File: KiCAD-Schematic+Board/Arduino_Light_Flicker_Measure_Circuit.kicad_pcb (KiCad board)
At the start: 2 copper layers, 35.6 x 113 mm, 35 parts, among them J1 Ds, J3 FTDI, J5 PWR(5V), Q1 BC547, Q2 BC547, U1 ATmega328P-PU, U2 AD5242, U3 AD823A, U4 Display

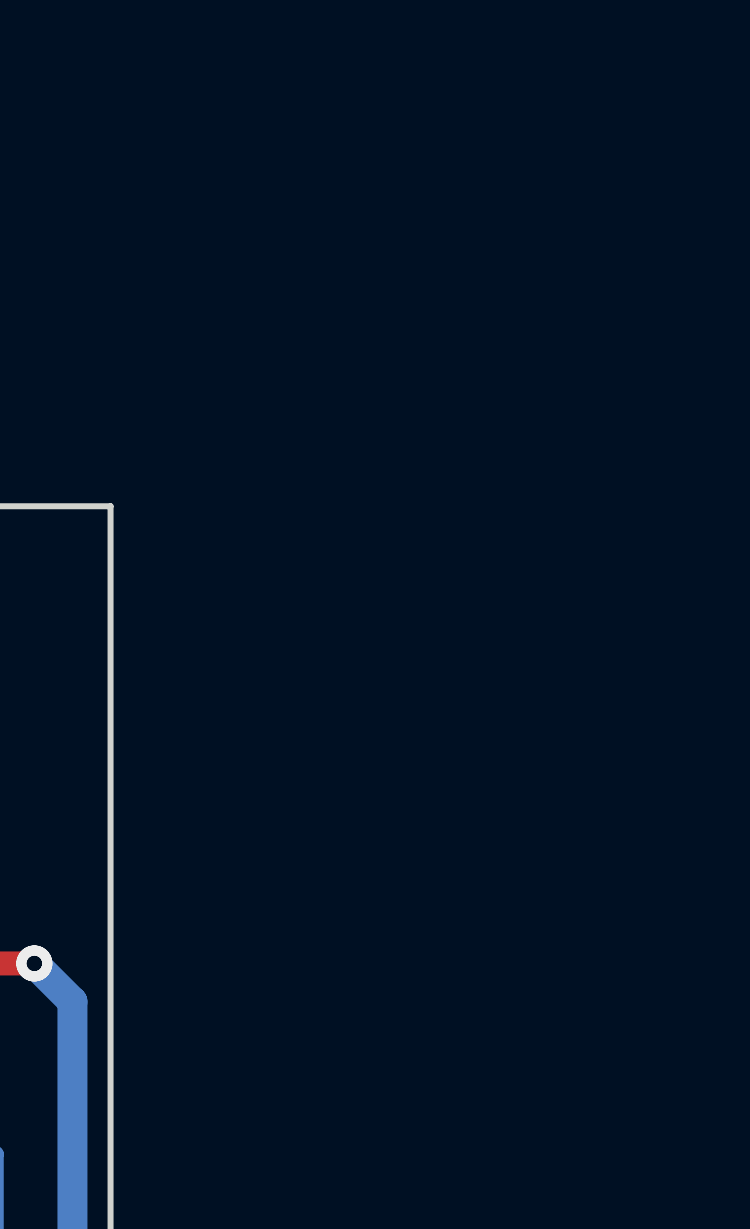
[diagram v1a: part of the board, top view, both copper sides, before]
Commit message: Add SSD1306 file, minor updates, also swapped two pins.  Slowly iterating.
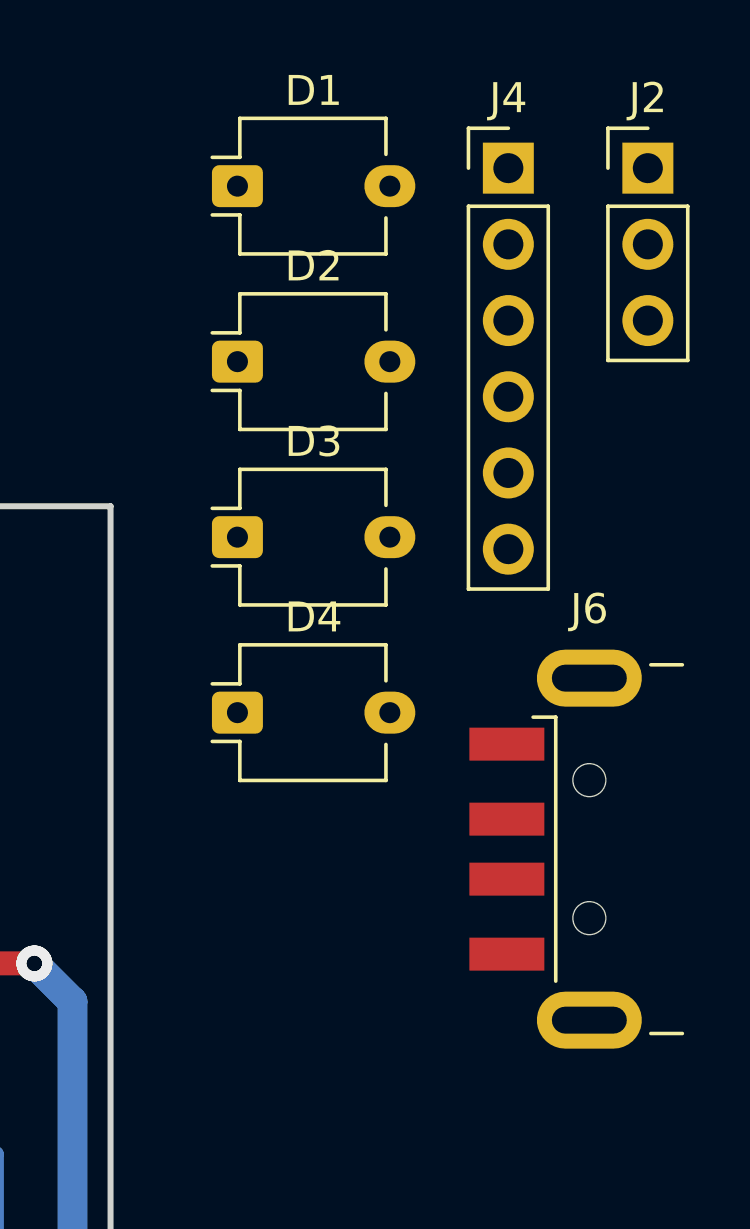
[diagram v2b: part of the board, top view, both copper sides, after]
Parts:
- added D1: BPW34, OptoDevice:Osram_DIL2_4.3x4.65mm_P5.08mm, F.Cu at (88.0, 55.4)
- added D2: BPW34, OptoDevice:Osram_DIL2_4.3x4.65mm_P5.08mm, F.Cu at (88.0, 61.2)
- added D3: BPW34, OptoDevice:Osram_DIL2_4.3x4.65mm_P5.08mm, F.Cu at (88.0, 67.1)
- added D4: BPW34, OptoDevice:Osram_DIL2_4.3x4.65mm_P5.08mm, F.Cu at (88.0, 72.9)
- added J2: Ds, Connector_PinHeader_2.54mm:PinHeader_1x03_P2.54mm_Vertical, F.Cu at (101.7, 54.8)
- added J4: FTDI-Conn, Connector_PinHeader_2.54mm:PinHeader_1x06_P2.54mm_Vertical, F.Cu at (97.1, 54.8)
- added J6: USB Power (5V), Connector_USB:USB_A_CNCTech_1001-011-01101_Horizontal, F.Cu at (106.7, 77.5)
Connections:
- net /TMR1-T1Clock renamed /T1
- J3 pad 4: Net-(J3-Pad4) -> unconnected-(J3-Pin_4-Pad4)
- U1 pad 12: Net-(U1-Pad12) -> unconnected-(U1-PD6-Pad12)
- U1 pad 13: Net-(U1-Pad13) -> unconnected-(U1-PD7-Pad13)
- U1 pad 14: Net-(U1-Pad14) -> unconnected-(U1-PB0-Pad14)
- U1 pad 15: Net-(U1-Pad15) -> unconnected-(U1-PB1-Pad15)
- U1 pad 16: Net-(U1-Pad16) -> unconnected-(U1-PB2-Pad16)
- U1 pad 17: Net-(U1-Pad17) -> unconnected-(U1-PB3-Pad17)
- U1 pad 18: Net-(U1-Pad18) -> unconnected-(U1-PB4-Pad18)
- U1 pad 19: Net-(U1-Pad19) -> unconnected-(U1-PB5-Pad19)
- U1 pad 24: Net-(U1-Pad24) -> unconnected-(U1-PC1-Pad24)
- U1 pad 25: Net-(U1-Pad25) -> unconnected-(U1-PC2-Pad25)
- U1 pad 26: Net-(U1-Pad26) -> unconnected-(U1-PC3-Pad26)
- U1 pad 4: Net-(U1-Pad4) -> unconnected-(U1-PD2-Pad4)
- U1 pad 5: Net-(U1-Pad5) -> unconnected-(U1-PD3-Pad5)
- U1 pad 6: Net-(U1-Pad6) -> unconnected-(U1-PD4-Pad6)
- U2 pad 1: Net-(U2-Pad1) -> unconnected-(U2-O1-Pad1)
- U2 pad 13: Net-(U2-Pad13) -> unconnected-(U2-O2-Pad13)
- U2 pad 16: Net-(U2-Pad16) -> unconnected-(U2-A2-Pad16)
- U2 pad 2: Net-(U2-Pad2) -> unconnected-(U2-A1-Pad2)
- U4 pad 2: GNDD -> +5V

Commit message: Update board setup to be mostly complete.  Still need to shrink and reorganize a bit.
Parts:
- removed J4: FTDI-Conn, Connector_PinHeader_2.54mm:PinHeader_1x06_P2.54mm_Vertical
- C1, C2: moved to B.Cu
- C100: renamed from 16MHz1; value Q -> 16MHz
- R1, R2: value 10k -> 10kΩ
- R11, R7, R9: value 1,5k -> 1.5kΩ
- R4: value 10k -> 10kΩ
- R5: value 1M -> 1MΩ
- R6: value 120k -> 120kΩ
- R8: value 1k -> 1kΩ
- moved J6 95.2 mm to (88.2, 170.8)
- moved J2 39.8 mm to (66.0, 72.4), turned to 90 degrees
- moved C9 5.46 mm to (59.1, 78.1), turned to 90 degrees
- moved C2 4.05 mm to (64.8, 156.2)
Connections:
- net /SCL renamed SCL
- net /SDA renamed SDA
- net /T1 renamed TMR1-T1Clock
- net GNDD renamed GND
- C9 pad 1: +5V -> Net-(U4-GND)
- U4 pad 1: +5V -> Net-(U4-GND)
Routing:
- net GND: track 298.4 -> 37.1 mm, vias 1 -> 0
- net +5V: track 222.1 -> 210.4 mm, vias 9 -> 2
- net SDA: track 107.2 -> 102.3 mm, vias 8 -> 3
- net Net-(U4-GND): track 0.00 -> 4.71 mm
- net Net-(U1-AREF): track 5.61 -> 9.98 mm
- net SCL: track 86.7 -> 84.1 mm, vias 8 -> 3
- net TMR1-T1Clock: track 136.9 -> 134.4 mm, vias 4 -> 2
- net Net-(J1-Pin_3): track 88.6 -> 87.5 mm, vias 7 -> 3
- net /ADC0: vias 4 -> 2

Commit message: Fix broken gitignore due to typo... Ouch.  Also clean up schematic even more, still need to do proper layout and BOM sourcing stuff.  Plus figure out the actual parts for the photodiodes still.
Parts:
- C1, C2, C3: value 100n -> 100nF
- R10: value 100k -> 100kΩ
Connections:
- net /ADC0 renamed ADC0
- C100 pad 1: Net-(U1-XTAL1/PB6) -> GND
- C4 pad 1: Net-(U1-XTAL1/PB6) -> GND
- U1 pad 9: Net-(U1-XTAL1/PB6) -> GND
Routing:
- net Net-(U1-XTAL1/PB6): track 12.3 -> 0.00 mm
- net GND: track 37.1 -> 49.4 mm

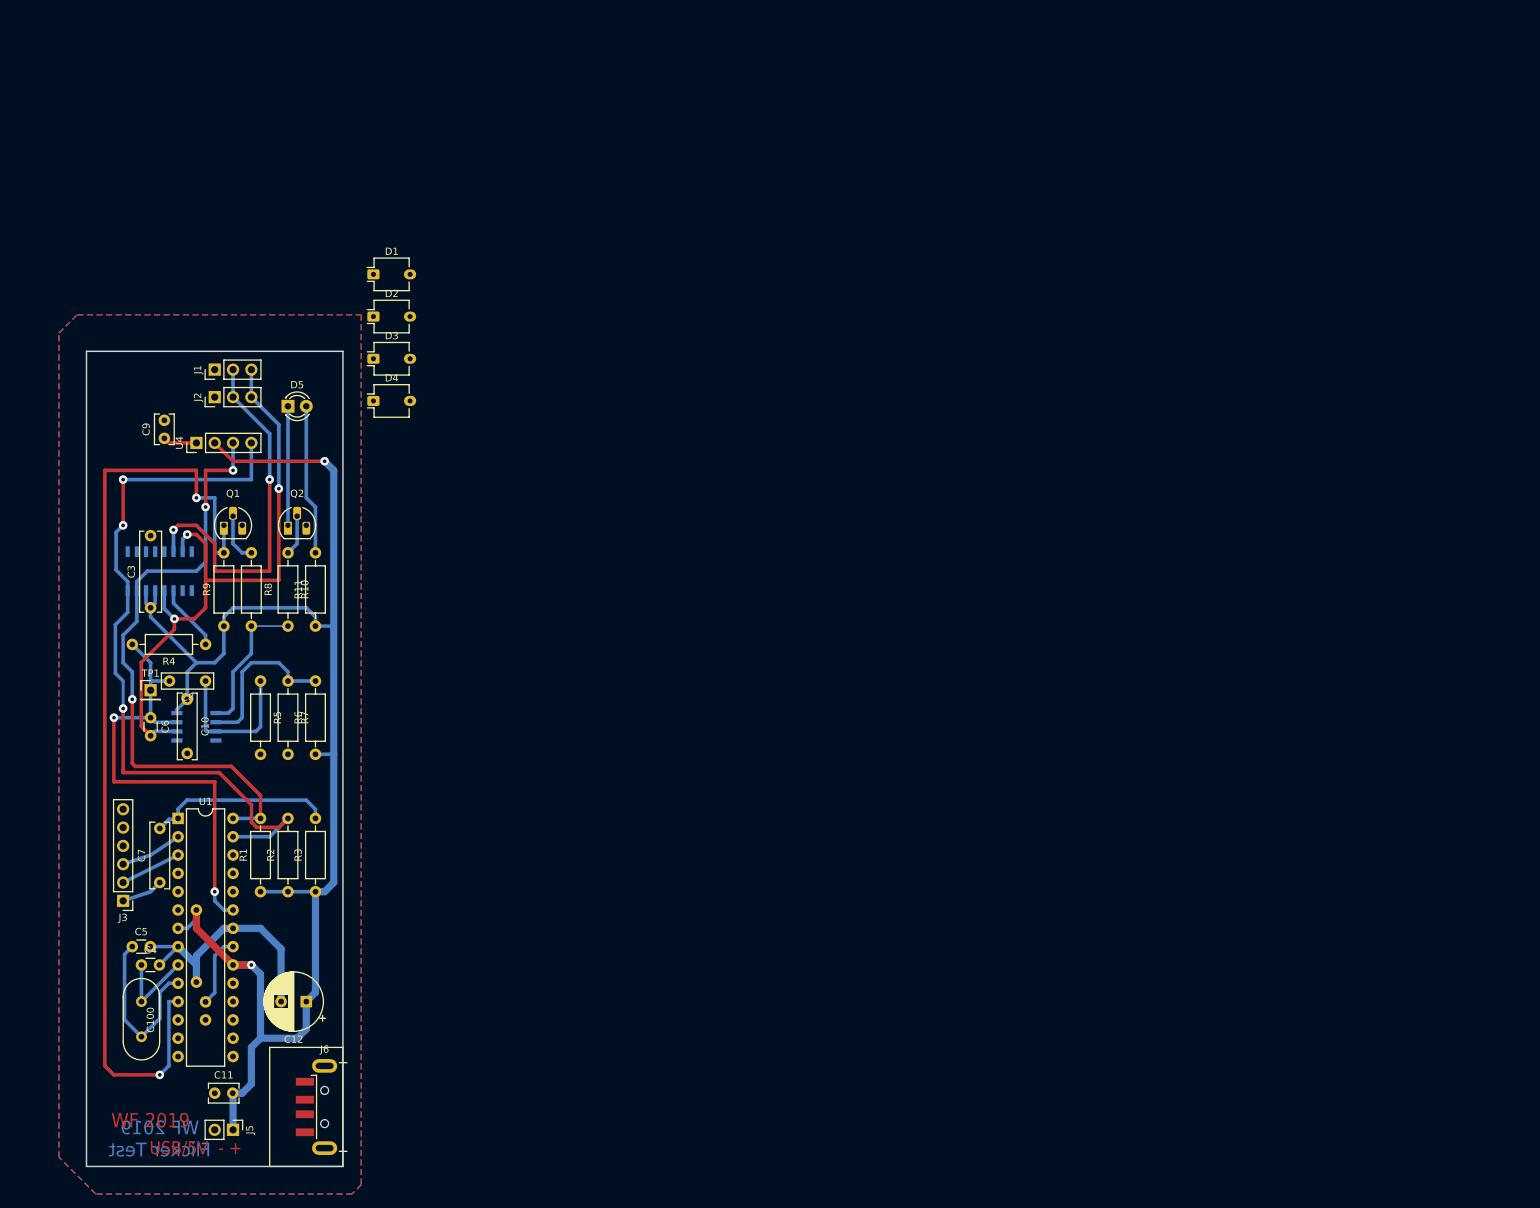
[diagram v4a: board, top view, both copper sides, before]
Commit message: Small update to add Pro Mini footprint to get rid of original footprint stuff hopefully.
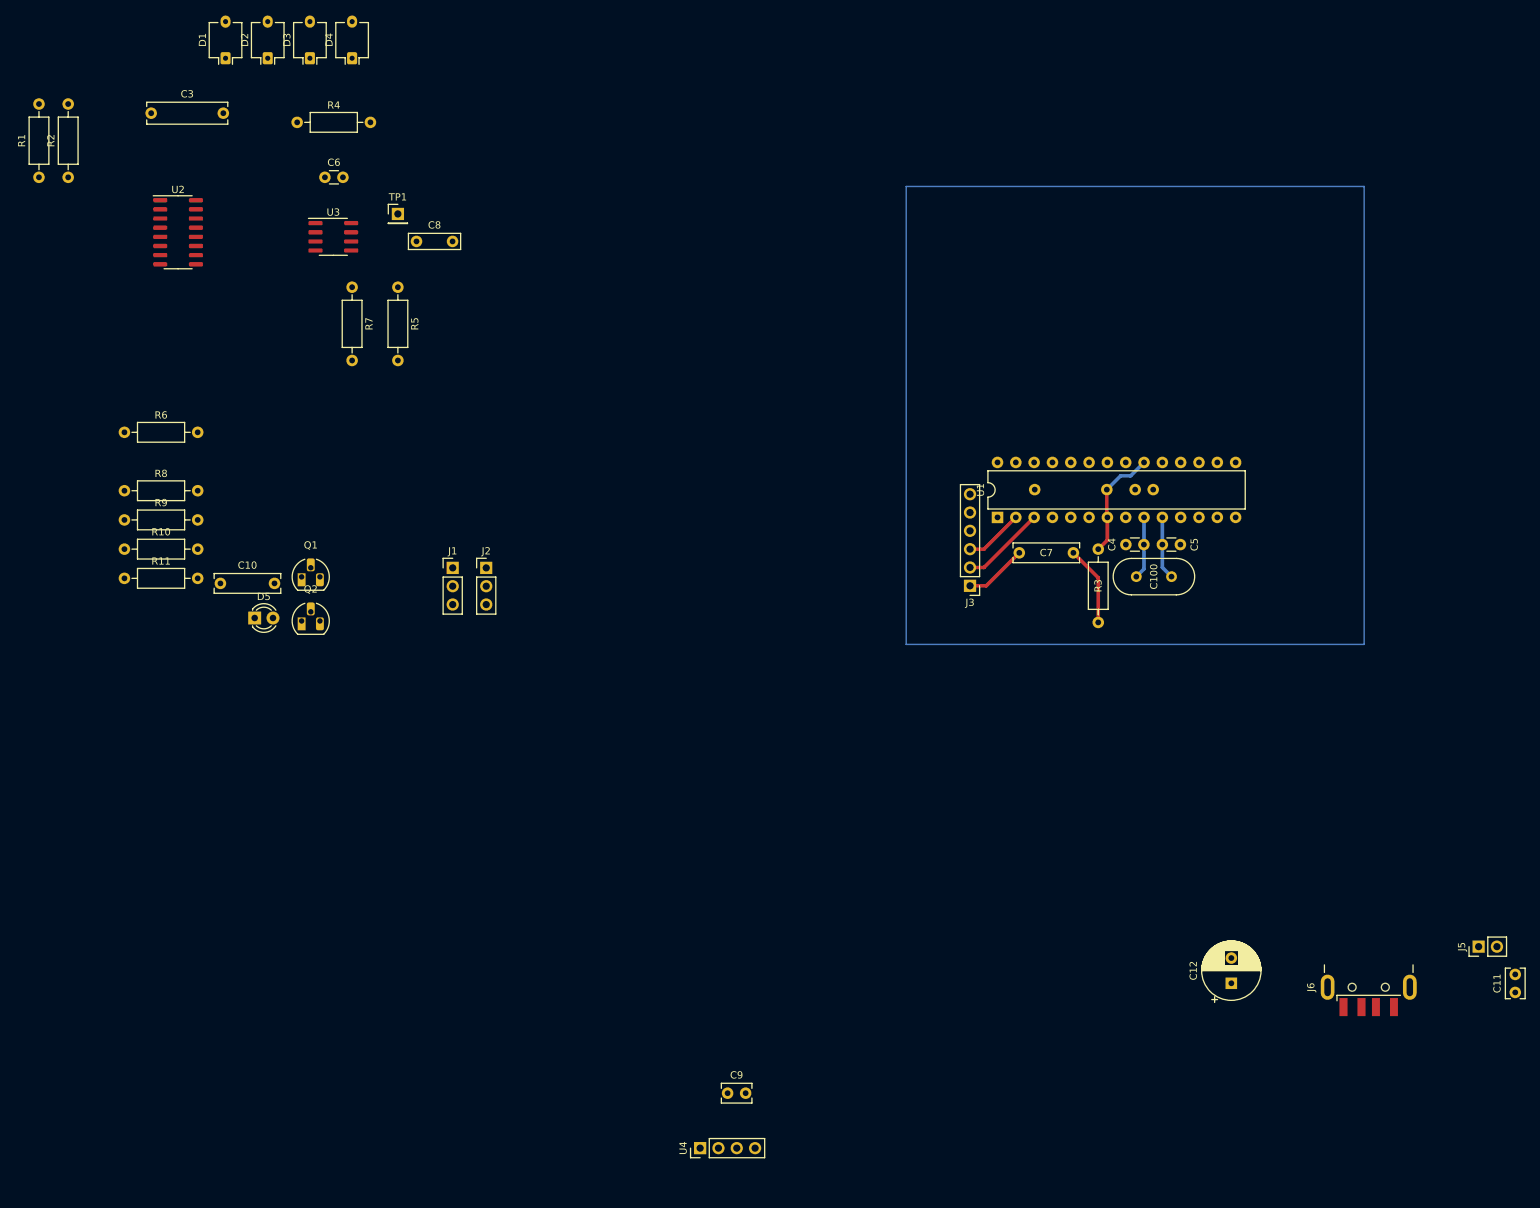
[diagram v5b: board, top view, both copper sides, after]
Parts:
- U2, U3: moved to F.Cu
- moved C11 180.9 mm to (246.4, 154.9), turned to 90 degrees
- moved J5 174.6 mm to (241.3, 148.6), turned to 90 degrees
- moved C5 153.3 mm to (197.4, 92.8)
- moved C4 150.7 mm to (194.9, 92.8), turned to 180 degrees
- moved C100 150.0 mm to (193.8, 97.3), turned to 0 degrees
- moved C2 147.2 mm to (193.7, 85.2), turned to 0 degrees
- moved J6 139.9 mm to (226.1, 147.3), turned to 90 degrees
- moved C1 139.1 mm to (189.7, 85.2), turned to 180 degrees
- moved C12 128.3 mm to (207.0, 153.7), turned to 90 degrees
- moved C7 127.7 mm to (177.6, 94.0), turned to 0 degrees
- moved J3 125.3 mm to (170.8, 98.6)
- moved U1 121.1 mm to (174.6, 89.1), turned to 90 degrees
- moved U4 120.2 mm to (133.3, 176.5)
- moved C9 119.8 mm to (137.2, 168.9), turned to 0 degrees
- moved R3 118.5 mm to (188.6, 93.5), turned to -90 degrees
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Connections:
- C100 pad 1: GND -> Net-(U1-XTAL1/PB6)
- C4 pad 1: GND -> Net-(U1-XTAL1/PB6)
- U1 pad 9: GND -> Net-(U1-XTAL1/PB6)
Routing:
- net +5V: track 210.4 -> 15.5 mm, vias 2 -> 0
- net TMR1-T1Clock: track 134.4 -> 0.00 mm, vias 2 -> 0
- net SDA: track 102.3 -> 0.00 mm, vias 3 -> 0
- net Net-(J1-Pin_3): track 87.5 -> 0.00 mm, vias 3 -> 0
- net SCL: track 84.1 -> 0.00 mm, vias 3 -> 0
- net ADC0: track 65.3 -> 0.00 mm, vias 2 -> 0
- net Net-(J1-Pin_2): track 51.5 -> 0.00 mm, vias 2 -> 0
- net GND: track 49.4 -> 0.00 mm
- net Net-(U3A--): track 22.7 -> 0.00 mm
- net Net-(U3A-+): track 21.1 -> 0.00 mm
- net Net-(D5-A): track 20.8 -> 0.00 mm
- net Net-(R10-Pad2): track 20.2 -> 0.00 mm
- net Net-(D5-K): track 16.5 -> 0.00 mm
- net Net-(U1-XTAL2/PB7): track 24.2 -> 8.74 mm
- net Net-(U1-~{RESET}/PC6): track 25.8 -> 11.1 mm
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- removed copper zone on B.Cu, net GND
- removed copper zone on F.Cu, net GND
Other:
- board outline removed
- board text removed: "USB/5V - +"
- board text removed: "WF 2019"
- board text removed: "WF 2019 Flicker Test"

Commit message: Update to do basic messed-up layout.  Imperfect but hopefully functional.
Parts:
- C10: moved to B.Cu
- moved C11 154.8 mm to (122.4, 62.2), turned to 0 degrees
- moved J5 142.2 mm to (125.7, 65.8), turned to -90 degrees
- moved U4 133.7 mm to (74.2, 56.6), turned to 0 degrees
- moved C9 124.7 mm to (77.6, 59.4), turned to -90 degrees
- moved J6 120.7 mm to (139.3, 63.3), turned to 0 degrees
- moved C12 117.1 mm to (123.0, 72.0), turned to 0 degrees
- moved C100 93.8 mm to (102.3, 76.9)
- moved C2 93.8 mm to (102.1, 64.8)
- moved J3 93.8 mm to (79.2, 78.2)
- moved U1 93.8 mm to (83.0, 68.7)
- moved C1 93.8 mm to (98.2, 64.8)
- moved C4 93.8 mm to (103.3, 72.5)
- moved C5 93.8 mm to (105.9, 72.5)
- moved C7 93.8 mm to (86.0, 73.6)
- moved R3 92.7 mm to (97.3, 77.2), turned to 180 degrees
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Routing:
- net +5V: track 15.5 -> 153.3 mm, vias 0 -> 1
- net ADC0: track 0.00 -> 47.0 mm, vias 0 -> 1
- net Net-(D1-A): track 0.00 -> 45.1 mm
- net Net-(J1-Pin_3): track 0.00 -> 41.2 mm, vias 0 -> 2
- net Net-(R10-Pad2): track 0.00 -> 37.2 mm, vias 0 -> 1
- net SCL: track 0.00 -> 30.3 mm
- net SDA: track 0.00 -> 27.1 mm
- net TMR1-T1Clock: track 0.00 -> 26.5 mm
- net Net-(U3A-+): track 0.00 -> 22.9 mm, vias 0 -> 1
- net Net-(U3A--): track 0.00 -> 21.3 mm
- net Net-(J1-Pin_2): track 0.00 -> 17.0 mm, vias 0 -> 1
- net Net-(U2-W1): track 0.00 -> 16.9 mm, vias 0 -> 1
- net Net-(Q2-B): track 0.00 -> 14.3 mm
- net Net-(D1-K): track 0.00 -> 13.5 mm
- net Net-(U1-~{RESET}/PC6): track 11.1 -> 21.2 mm
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- added copper zone on B.Cu, net GND
- added copper zone on F.Cu, net GND
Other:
- board outline added: 65.3 x 43.2 mm
- board text added: "flicker? i hardly know'er"
